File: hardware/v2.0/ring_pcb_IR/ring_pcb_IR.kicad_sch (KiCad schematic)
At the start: 22 parts, among them Q1 Q_PNP_BEC, Q2 Q_Dual_NPN_NPN_C2E2C1E1B1B2, Q3 Q_Dual_NPN_NPN_C2E2C1E1B1B2, U2 ATtiny85-20M

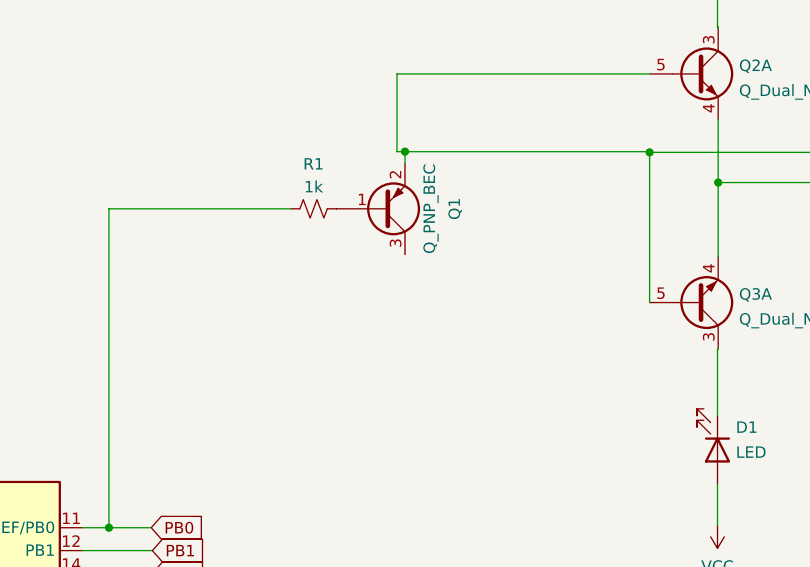
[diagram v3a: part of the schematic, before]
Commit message: Add collector connection for PNP
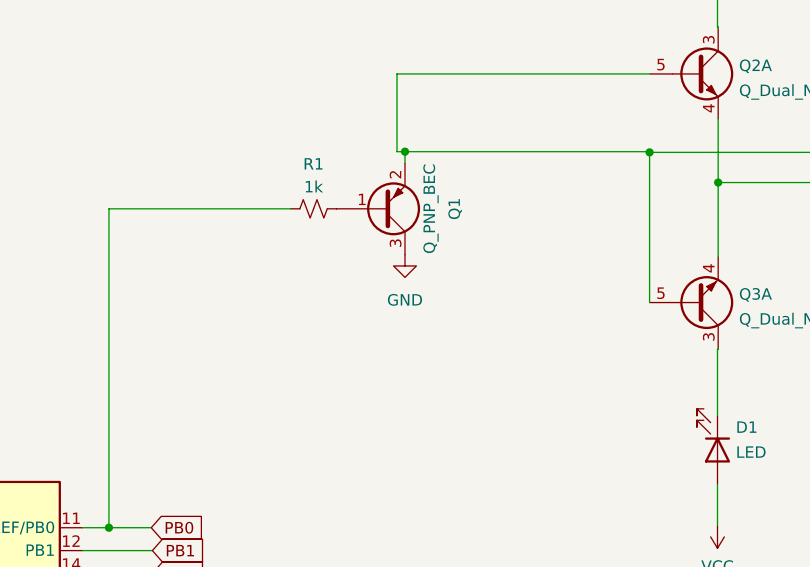
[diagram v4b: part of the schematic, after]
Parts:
- C1: MPN (none) -> C0603C104J4RACTU
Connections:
- net GND: now also Q1.3 (C)
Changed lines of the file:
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@@
+      (effects (font (size 1.27 1.27)) hide)
+    )
+    (property "MPN" "" (at 223.4692 29.2608 0)
       (effects (font (size 1.27 1.27)) hide)
     )
@@
       (effects (font (size 1.27 1.27)) hide)
     )
+    (property "MPN" "" (at 87.249 138.557 0)
+      (effects (font (size 1.27 1.27)) hide)
+    )
     (pin "1")
     (instances
@@
       (effects (font (size 1.27 1.27)) hide)
     )
+    (property "MPN" "C0603C104J4RACTU" (at 95.631 60.96 0)
+      (effects (font (size 1.27 1.27)) hide)
+    )
     (pin "1")
     (pin "2")
@@
       (effects (font (size 1.27 1.27)) hide)
     )
+    (property "MPN" "" (at 108.839 138.43 0)
+      (effects (font (size 1.27 1.27)) hide)
+    )
     (pin "1")
     (instances
@@
       (effects (font (size 1.27 1.27)) hide)
     )
+    (property "MPN" "" (at 87.503 147.32 0)
+      (effects (font (size 1.27 1.27)) hide)
+    )
     (pin "1")
     (instances
@@
       (effects (font (size 1.27 1.27)) hide)
     )
+    (property "MPN" "" (at 179.07 120.65 0)
+      (effects (font (size 1.27 1.27)) hide)
+    )
     (pin "1")
     (pin "2")
@@
     )
     (property "Datasheet" "~" (at 106.553 138.43 0)
+      (effects (font (size 1.27 1.27)) hide)
+    )
+    (property "MPN" "" (at 101.473 138.43 0)
       (effects (font (size 1.27 1.27)) hide)
     )
@@
     )
     (property "Datasheet" "http://ww1.microchip.com/downloads/en/DeviceDoc/atmel-2586-avr-8-bit-microcontroller-attiny25-attiny45-attiny85_datasheet.pdf" (at 112.395 103.886 0)
+      (effects (font (size 1.27 1.27)) hide)
+    )
+    (property "MPN" "" (at 112.395 103.886 0)
       (effects (font (size 1.27 1.27)) hide)
     )
@@
       (effects (font (size 1.27 1.27)) hide)
     )
+    (property "MPN" "" (at 153.289 60.833 0)
+      (effects (font (size 1.27 1.27)) hide)
+    )
     (pin "1")
     (pin "2")
@@
     )
     (property "Datasheet" "~" (at 220.853 45.593 0)
+      (effects (font (size 1.27 1.27)) hide)
+    )
+    (property "MPN" "" (at 220.853 45.593 0)
       (effects (font (size 1.27 1.27)) hide)
     )
@@
       (effects (font (size 1.27 1.27)) hide)
     )
+    (property "MPN" "" (at 104.013 147.447 0)
+      (effects (font (size 1.27 1.27)) hide)
+    )
     (pin "1")
     (instances
@@
     )
     (property "Datasheet" "~" (at 220.98 71.247 0)
+      (effects (font (size 1.27 1.27)) hide)
+    )
+    (property "MPN" "" (at 220.98 71.247 0)
       (effects (font (size 1.27 1.27)) hide)
     )
@@
       (effects (font (size 1.27 1.27)) hide)
     )
+    (property "MPN" "" (at 198.1708 29.2608 0)
+      (effects (font (size 1.27 1.27)) hide)
+    )
     (pin "1")
     (pin "2")
@@
     )
     (property "Datasheet" "~" (at 195.707 45.847 0)
+      (effects (font (size 1.27 1.27)) hide)
+    )
+    (property "MPN" "" (at 195.707 45.847 0)
       (effects (font (size 1.27 1.27)) hide)
     )
@@
       (effects (font (size 1.27 1.27)) hide)
     )
+    (property "MPN" "" (at 73.406 138.684 0)
+      (effects (font (size 1.27 1.27)) hide)
+    )
     (pin "1")
     (instances
@@
       (effects (font (size 1.27 1.27)) hide)
     )
+    (property "MPN" "" (at 223.4692 87.7824 0)
+      (effects (font (size 1.27 1.27)) hide)
+    )
     (pin "1")
     (pin "2")
@@
       (effects (font (size 1.27 1.27)) hide)
     )
+    (property "MPN" "" (at 170.561 120.65 0)
+      (effects (font (size 1.27 1.27)) hide)
+    )
     (pin "1")
     (pin "2")
@@
       (effects (font (size 1.27 1.27)) hide)
     )
+    (property "MPN" "" (at 105.156 60.96 0)
+      (effects (font (size 1.27 1.27)) hide)
+    )
     (pin "1")
     (pin "2")
@@
       (effects (font (size 1.27 1.27)) hide)
     )
+    (property "MPN" "" (at 58.928 147.066 0)
+      (effects (font (size 1.27 1.27)) hide)
+    )
     (pin "1")
     (instances
@@
     )
     (property "Datasheet" "~" (at 68.326 147.32 0)
+      (effects (font (size 1.27 1.27)) hide)
+    )
+    (property "MPN" "" (at 73.406 147.32 0)
       (effects (font (size 1.27 1.27)) hide)
     )
@@
       (effects (font (size 1.27 1.27)) hide)
     )
+    (property "MPN" "" (at 198.1708 87.63 0)
+      (effects (font (size 1.27 1.27)) hide)
+    )
     (pin "1")
     (pin "2")
@@
     )
     (property "Datasheet" "~" (at 195.707 71.247 0)
+      (effects (font (size 1.27 1.27)) hide)
+    )
+    (property "MPN" "" (at 195.707 71.247 0)
       (effects (font (size 1.27 1.27)) hide)
     )
@@
       (effects (font (size 1.27 1.27)) hide)
     )
+    (property "MPN" "" (at 59.055 138.938 0)
+      (effects (font (size 1.27 1.27)) hide)
+    )
     (pin "1")
     (instances
@@
       (effects (font (size 1.27 1.27)) hide)
     )
+    (property "MPN" "" (at 160.909 60.833 0)
+      (effects (font (size 1.27 1.27)) hide)
+    )
     (pin "1")
     (pin "2")
@@
         )
       )
+    )
+  )
+  (symbol (lib_id "power:GND") (at 163.449 65.913 0) (unit 1)
+    (in_bom yes) (on_board yes) (dnp no)
+    (property "Reference" "#PWR09" (at 163.449 72.263 0)
+      (effects (font (size 1.27 1.27)) hide)
+    )
+    (property "Value" "GND" (at 163.449 70.993 0)
+      (effects (font (size 1.27 1.27)))
+    )
+    (property "Footprint" "" (at 163.449 65.913 0)
+      (effects (font (size 1.27 1.27)) hide)
+    )
+    (property "Datasheet" "" (at 163.449 65.913 0)
+      (effects (font (size 1.27 1.27)) hide)
+    )
+    (pin "1")
+    (instances
+      (project "ring_pcb_IR"
+        (path "/e63e39d7-6ac0-4ffd-8aa3-1841a4541b55"
+          (reference "#PWR09") (unit 1)
+        )
+      )

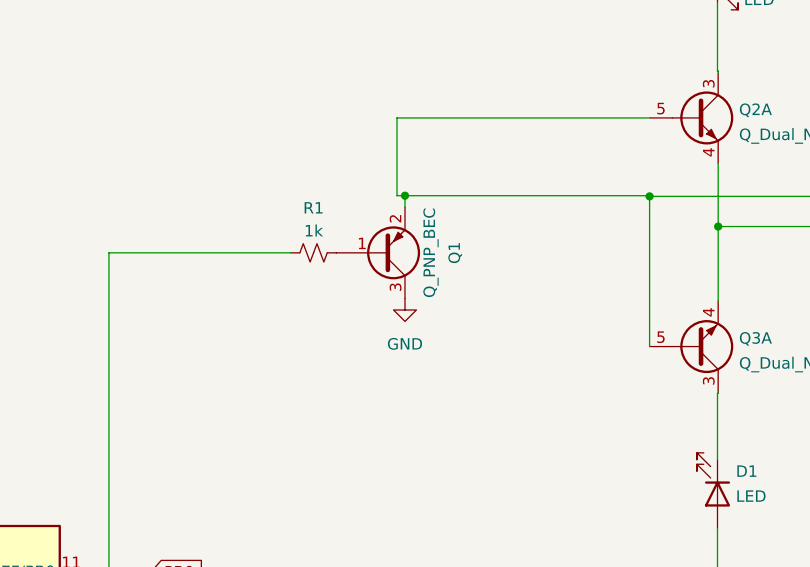
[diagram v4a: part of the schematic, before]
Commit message: Routed with smaller PCB
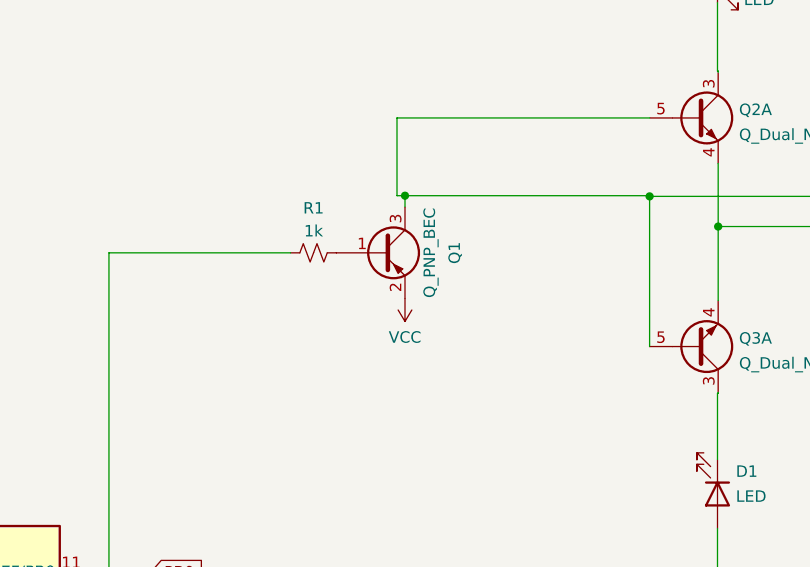
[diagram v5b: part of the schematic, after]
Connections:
- net GND: no longer Q1.3 (C)
- net VCC: now also Q1.2 (E)
- net at Q2.5 (B1), Q2.6 (B2), Q3.5 (B1)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: now also Q1.3 (C); no longer Q1.2 (E)
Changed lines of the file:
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@@
     )
   )
-  (symbol (lib_id "Device:Q_PNP_BEC") (at 160.909 60.833 0) (mirror x) (unit 1)
+  (symbol (lib_id "Device:Q_PNP_BEC") (at 160.909 60.833 0) (unit 1)
     (in_bom yes) (on_board yes) (dnp no)
     (property "Reference" "Q1" (at 168.9649 60.833 90)
@@
       (effects (font (size 1.27 1.27)))
     )
-    (property "Footprint" "Package_TO_SOT_SMD:SOT-23" (at 165.989 63.373 0)
+    (property "Footprint" "Package_TO_SOT_SMD:SOT-23" (at 165.989 58.293 0)
       (effects (font (size 1.27 1.27)) hide)
     )
@@
     )
   )
-  (symbol (lib_id "power:GND") (at 163.449 65.913 0) (unit 1)
-    (in_bom yes) (on_board yes) (dnp no)
-    (property "Reference" "#PWR09" (at 163.449 72.263 0)
+  (symbol (lib_name "VCC_1") (lib_id "power:VCC") (at 163.449 65.913 180) (unit 1)
+    (in_bom yes) (on_board yes) (dnp no) (fields_autoplaced)
+    (property "Reference" "#PWR09" (at 163.449 62.103 0)
       (effects (font (size 1.27 1.27)) hide)
     )
-    (property "Value" "GND" (at 163.449 70.993 0)
+    (property "Value" "VCC" (at 163.449 70.231 0)
       (effects (font (size 1.27 1.27)))
     )

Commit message: Choose LED's
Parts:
- D1, D2, D3, D4: MPN (none) -> 15406094BA500
- D5: MPN (none) -> 150060RS75000
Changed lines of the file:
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@@
       (effects (font (size 1.27 1.27)) hide)
     )
-    (property "MPN" "" (at 223.4692 29.2608 0)
+    (property "MPN" "15406094BA500" (at 223.4692 29.2608 0)
       (effects (font (size 1.27 1.27)) hide)
     )
@@
       (effects (font (size 1.27 1.27)) hide)
     )
-    (property "MPN" "" (at 179.07 120.65 0)
+    (property "MPN" "150060RS75000" (at 179.07 120.65 0)
       (effects (font (size 1.27 1.27)) hide)
     )
@@
       (effects (font (size 1.27 1.27)) hide)
     )
-    (property "MPN" "" (at 198.1708 29.2608 0)
+    (property "MPN" "15406094BA500" (at 198.1708 29.2608 0)
       (effects (font (size 1.27 1.27)) hide)
     )
@@
       (effects (font (size 1.27 1.27)) hide)
     )
-    (property "MPN" "" (at 223.4692 87.7824 0)
+    (property "MPN" "15406094BA500" (at 223.4692 87.7824 0)
       (effects (font (size 1.27 1.27)) hide)
     )
@@
       (effects (font (size 1.27 1.27)) hide)
     )
-    (property "MPN" "" (at 198.1708 87.63 0)
-      (effects (font (size 1.27 1.27)) hide)
-    )
+    (property "MPN" "15406094BA500" (at 198.1708 87.63 0)
+      (effects (font (size 1.27 1.27)) hide)
+    )

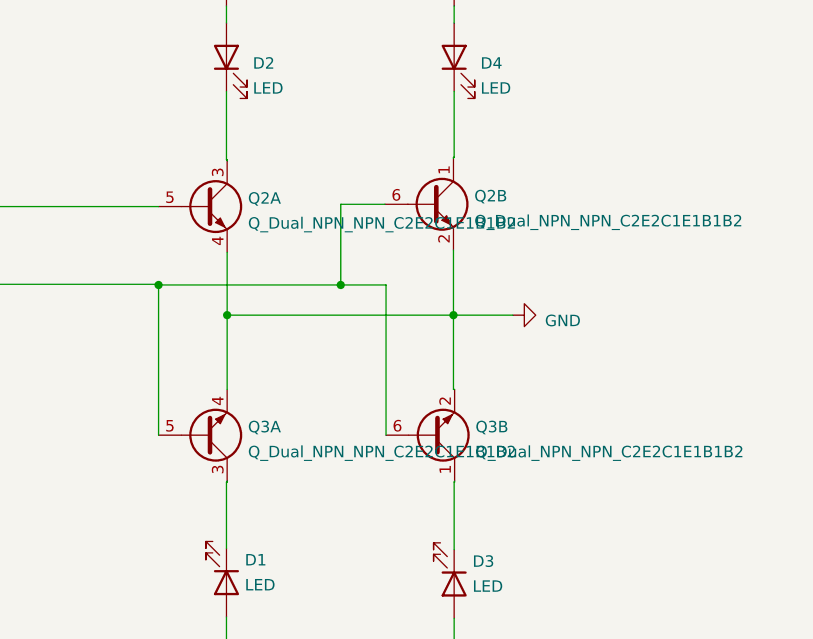
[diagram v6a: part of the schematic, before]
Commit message: Change transistors and rewire
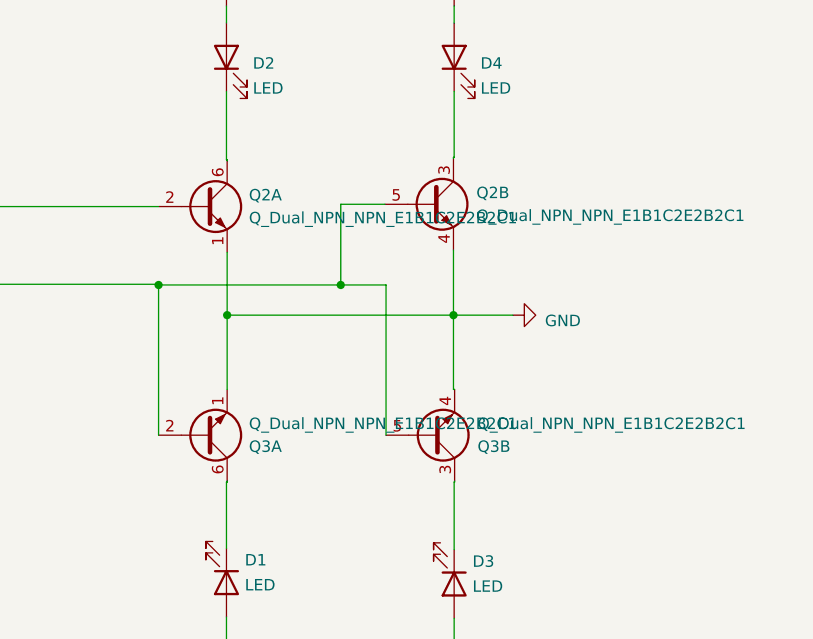
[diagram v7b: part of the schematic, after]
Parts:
- removed Q2, Q3: Q_Dual_NPN_NPN_C2E2C1E1B1B2, Package_TO_SOT_SMD:SOT-23-6, symbol Device:Q_Dual_NPN_NPN_C2E2C1E1B1B2
- added Q2, Q3: Q_Dual_NPN_NPN_E1B1C2E2B2C1, Package_TO_SOT_SMD:SOT-363_SC-70-6, symbol Device:Q_Dual_NPN_NPN_E1B1C2E2B2C1
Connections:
- net GND: now also Q2.1 (E1), Q2.4 (E2), Q3.1 (E1), Q3.4 (E2)
- net at D4.1 (K): now also Q2.3 (C2)
- net at Q1.3 (C): now also Q2.2 (B1), Q2.5 (B2), Q3.2 (B1), Q3.5 (B2)
- net at D3.1 (K): now also Q3.3 (C2)
- net at D2.1 (K): now also Q2.6 (C1)
- net at D1.1 (K): now also Q3.6 (C1)

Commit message: Select more parts
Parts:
- R1: MPN (none) -> RT0603FRE101KL
- R2: MPN (none) -> RT0603BRD07210RL
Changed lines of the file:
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@@
       (effects (font (size 1.27 1.27)) hide)
     )
-    (property "Datasheet" "~" (at 153.289 60.833 0)
+    (property "Datasheet" "https://au.mouser.com/datasheet/2/447/PYu_RT_1_to_0_01_RoHS_L_12-3003070.pdf" (at 153.289 60.833 0)
       (effects (font (size 1.27 1.27)) hide)
     )
-    (property "MPN" "" (at 153.289 60.833 0)
+    (property "MPN" "RT0603FRE101KL" (at 153.289 60.833 0)
       (effects (font (size 1.27 1.27)) hide)
     )
@@
       (effects (font (size 1.27 1.27)) hide)
     )
-    (property "Datasheet" "~" (at 170.561 120.65 0)
+    (property "Datasheet" "https://au.mouser.com/datasheet/2/447/PYu_RT_1_to_0_01_RoHS_L_12-3003070.pdf" (at 170.561 120.65 0)
       (effects (font (size 1.27 1.27)) hide)
     )
-    (property "MPN" "" (at 170.561 120.65 0)
+    (property "MPN" "RT0603BRD07210RL" (at 170.561 120.65 0)
       (effects (font (size 1.27 1.27)) hide)
     )
